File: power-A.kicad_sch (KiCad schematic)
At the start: 28 parts, among them J201 PCB Receptacle, J202 PCB Receptacle, J203 Conn_01x05, U201 AMS1117-ADJ_SOT223

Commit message: Pre routing: footprints&parts
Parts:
- D201: value SMBJ170CA -> TVS Diode; JLCPCB C114013 -> C78395
- D204: value MDD SS14 -> B5819W; footprint Diode_SMD:D_SMA -> Diode_SMD:D_SOD-123; JLCPCB C2480 -> C8598
- D205, D206: value SM4007PL -> B5819W; JLCPCB C64898 -> C8598
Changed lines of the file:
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@@
       (effects (font (size 1.27 1.27)) (justify right))
     )
-    (property "Value" "SMBJ170CA" (id 1) (at 38.735 85.725 0)
+    (property "Value" "TVS Diode" (id 1) (at 38.735 85.725 0)
       (effects (font (size 1.27 1.27)) (justify right))
     )
@@
       (effects (font (size 1.27 1.27)) hide)
     )
-    (property "JLCPCB" "C114013" (id 4) (at 41.91 91.44 0)
+    (property "JLCPCB" "C78395" (id 4) (at 41.91 91.44 0)
       (effects (font (size 1.27 1.27)) hide)
     )
@@
       (effects (font (size 1.27 1.27)) (justify left))
     )
-    (property "Value" "SM4007PL" (id 1) (at 171.45 139.6999 90)
+    (property "Value" "B5819W" (id 1) (at 171.45 139.6999 90)
       (effects (font (size 1.27 1.27)) (justify left))
     )
@@
       (effects (font (size 1.27 1.27)) hide)
     )
-    (property "JLCPCB" "C64898" (id 4) (at 168.275 138.43 0)
+    (property "JLCPCB" "C8598 " (id 4) (at 168.275 138.43 0)
       (effects (font (size 1.27 1.27)) hide)
     )
@@
       (effects (font (size 1.27 1.27)) (justify left))
     )
-    (property "Value" "SM4007PL" (id 1) (at 171.45 129.5399 90)
+    (property "Value" "B5819W" (id 1) (at 171.45 129.5399 90)
       (effects (font (size 1.27 1.27)) (justify left))
     )
@@
       (effects (font (size 1.27 1.27)) hide)
     )
-    (property "JLCPCB" "C64898" (id 4) (at 168.275 128.27 0)
+    (property "JLCPCB" "C8598 " (id 4) (at 168.275 128.27 0)
       (effects (font (size 1.27 1.27)) hide)
     )
@@
     (in_bom yes) (on_board yes)
     (property "Reference" "D204" (id 0) (at 112.395 76.835 0))
-    (property "Value" "MDD SS14" (id 1) (at 111.76 83.82 0))
-    (property "Footprint" "Diode_SMD:D_SMA" (id 2) (at 112.395 80.645 0)
-      (effects (font (size 1.27 1.27)) hide)
-    )
-    (property "Datasheet" "https://datasheet.lcsc.com/lcsc/2204121115_MDD-Microdiode-Electronics--SS14_C2480.pdf" (id 3) (at 112.395 80.645 0)
-      (effects (font (size 1.27 1.27)) hide)
-    )
-    (property "JLCPCB" "C2480" (id 4) (at 112.395 80.645 0)
-      (effects (font (size 1.27 1.27)) hide)
-    )
+    (property "Value" "B5819W" (id 1) (at 111.76 83.82 0))
+    (property "Footprint" "Diode_SMD:D_SOD-123" (id 2) (at 112.395 80.645 0)
+      (effects (font (size 1.27 1.27)) hide)
+    )
+    (property "Datasheet" "" (id 3) (at 112.395 80.645 0)
+      (effects (font (size 1.27 1.27)) hide)
+    )
+    (property "JLCPCB" "C8598 " (id 4) (at 112.395 80.645 0)
+      (effects (font (size 1.27 1.27)) hide)
+    )

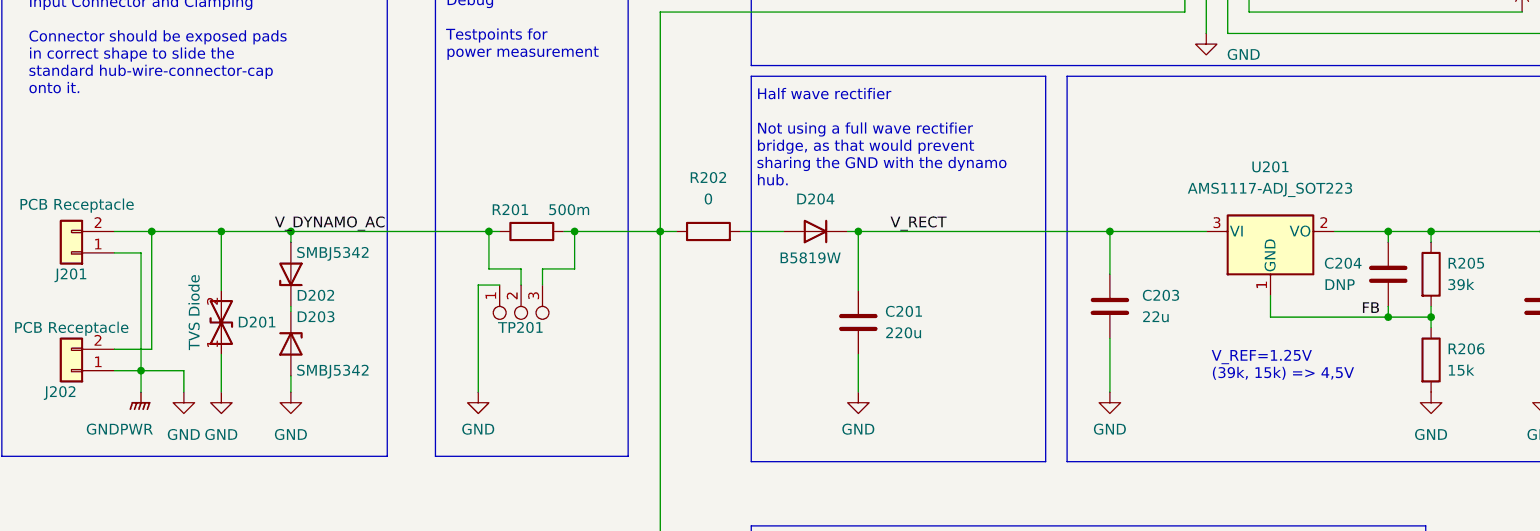
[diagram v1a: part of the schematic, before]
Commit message: Schematics: Add mountingpins to connectors, remove ERC warnings for alternate parts
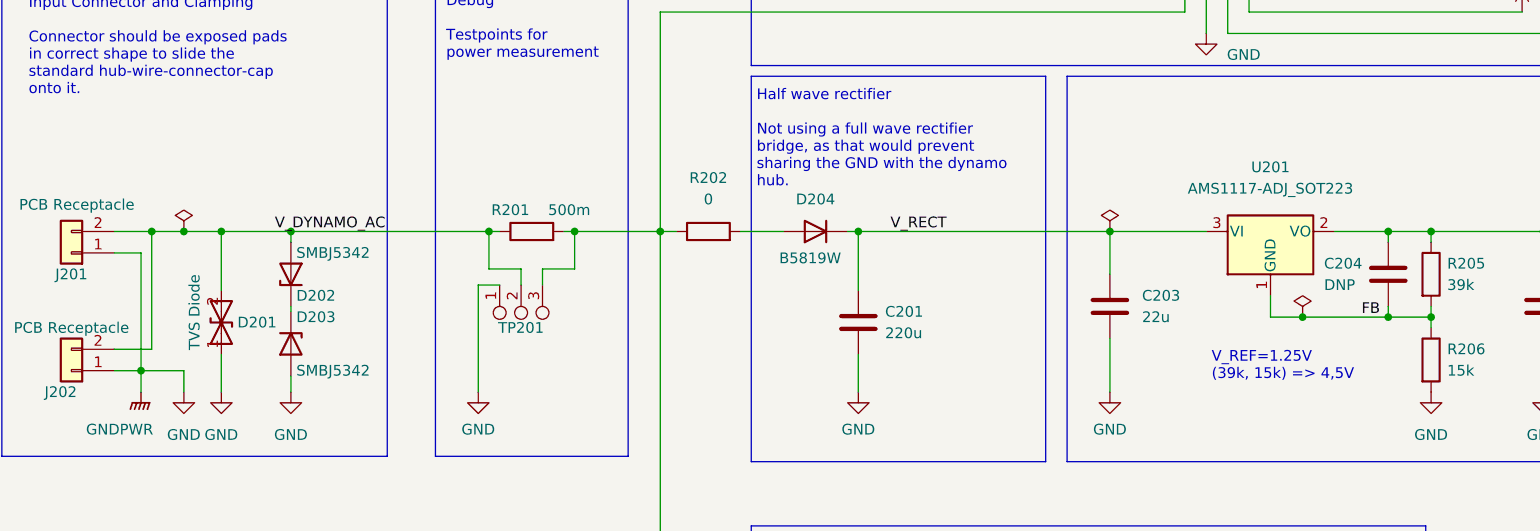
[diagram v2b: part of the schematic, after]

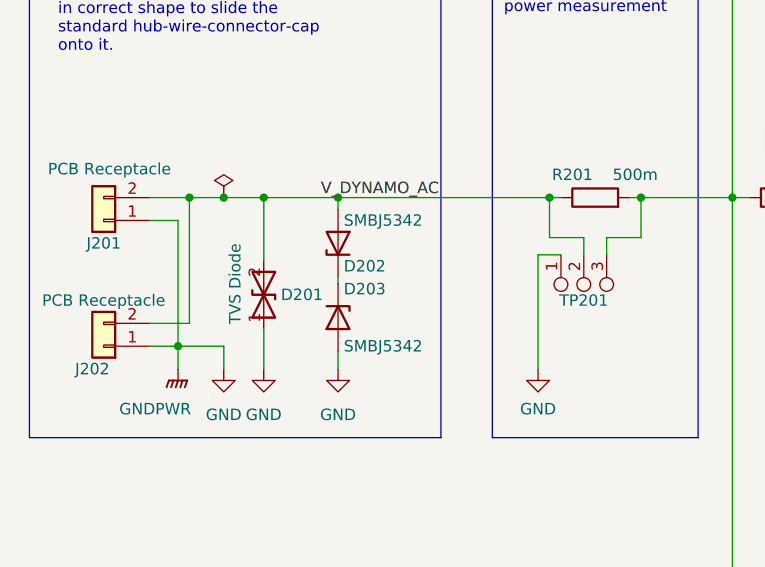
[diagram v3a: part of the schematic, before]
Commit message: schematic: cleanups and diode selection
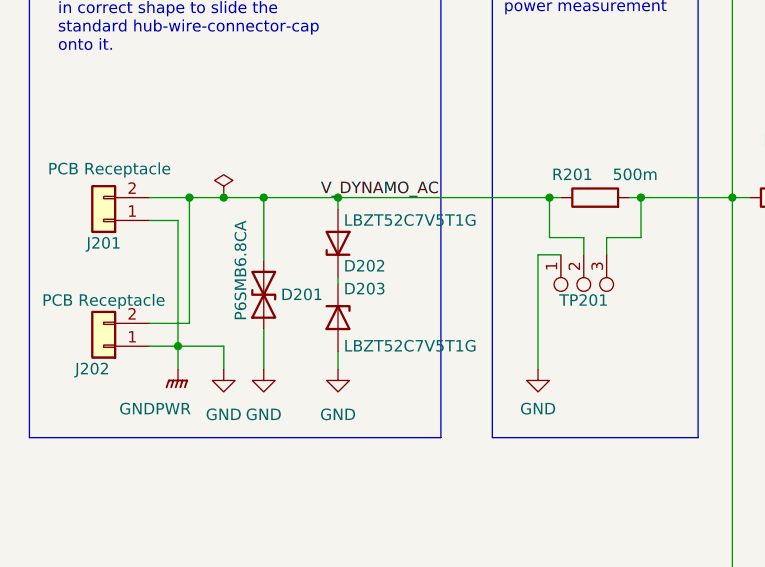
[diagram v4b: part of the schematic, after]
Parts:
- D201: value TVS Diode -> P6SMB6.8CA
- D202, D203: value SMBJ5342 -> LBZT52C7V5T1G; footprint Diode_SMD:D_SMB -> Diode_SMD:D_SOD-123; JLCPCB C132286 -> C12760
- U201: JLCPCB (none) -> C347224
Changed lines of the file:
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@@
       (effects (font (size 1.27 1.27)) (justify left))
     )
-    (property "Value" "SMBJ5342" (id 1) (at 50.8 97.155 90)
-      (effects (font (size 1.27 1.27)) (justify left))
-    )
-    (property "Footprint" "Diode_SMD:D_SMB" (id 2) (at 50.165 93.98 0)
+    (property "Value" "LBZT52C7V5T1G" (id 1) (at 50.8 97.155 90)
+      (effects (font (size 1.27 1.27)) (justify left))
+    )
+    (property "Footprint" "Diode_SMD:D_SOD-123" (id 2) (at 50.165 93.98 0)
       (effects (font (size 1.27 1.27)) hide)
     )
@@
       (effects (font (size 1.27 1.27)) hide)
     )
-    (property "JLCPCB" "C132286" (id 4) (at 50.165 93.98 0)
+    (property "JLCPCB" "C12760" (id 4) (at 50.165 93.98 0)
       (effects (font (size 1.27 1.27)) hide)
     )
@@
       (effects (font (size 1.27 1.27)) (justify right))
     )
-    (property "Value" "TVS Diode" (id 1) (at 38.735 85.725 0)
+    (property "Value" "P6SMB6.8CA" (id 1) (at 39.37 83.185 0)
       (effects (font (size 1.27 1.27)) (justify right))
     )
@@
       (effects (font (size 1.27 1.27)) hide)
     )
-    (property "Datasheet" "" (id 3) (at 168.91 86.995 0)
+    (property "Datasheet" "~" (id 3) (at 168.91 86.995 0)
+      (effects (font (size 1.27 1.27)) hide)
+    )
+    (property "JLCPCB" "C347224" (id 4) (at 166.37 80.645 0)
       (effects (font (size 1.27 1.27)) hide)
     )
@@
       (effects (font (size 1.27 1.27)) hide)
     )
-    (property "Datasheet" "" (id 3) (at 168.275 138.43 0)
+    (property "Datasheet" "~" (id 3) (at 168.275 138.43 0)
       (effects (font (size 1.27 1.27)) hide)
     )
@@
       (effects (font (size 1.27 1.27)) (justify right))
     )
-    (property "Value" "SMBJ5342" (id 1) (at 50.8 83.185 90)
-      (effects (font (size 1.27 1.27)) (justify right))
-    )
-    (property "Footprint" "Diode_SMD:D_SMB" (id 2) (at 50.165 85.725 0)
+    (property "Value" "LBZT52C7V5T1G" (id 1) (at 50.8 83.185 90)
+      (effects (font (size 1.27 1.27)) (justify right))
+    )
+    (property "Footprint" "Diode_SMD:D_SOD-123" (id 2) (at 50.165 85.725 0)
       (effects (font (size 1.27 1.27)) hide)
     )
@@
       (effects (font (size 1.27 1.27)) hide)
     )
-    (property "JLCPCB" "C132286" (id 4) (at 50.165 85.725 0)
+    (property "JLCPCB" "C12760" (id 4) (at 50.165 85.725 0)
       (effects (font (size 1.27 1.27)) hide)
     )
@@
       (effects (font (size 1.27 1.27)) hide)
     )
-    (property "Datasheet" "" (id 3) (at 168.275 128.27 0)
+    (property "Datasheet" "~" (id 3) (at 168.275 128.27 0)
       (effects (font (size 1.27 1.27)) hide)
     )
@@
       (effects (font (size 1.27 1.27)) hide)
     )
-    (property "Datasheet" "" (id 3) (at 112.395 80.645 0)
-      (effects (font (size 1.27 1.27)) hide)
-    )
+    (property "Datasheet" "~" (id 3) (at 112.395 80.645 0)
+      (effects (font (size 1.27 1.27)) hide)
+    )

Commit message: footprints: define testpoint with smaller courtyard
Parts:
- TP201, TP202: footprint Connector_PinHeader_1.27mm:PinHeader_1x03_P1.27mm_Vertical -> project-lib:TestPoint_1x03_P1.27mm
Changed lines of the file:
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@@
       (effects (font (size 1.27 1.27)) hide)
     )
-    (property "Footprint" "Connector_PinHeader_1.27mm:PinHeader_1x03_P1.27mm_Vertical" (id 2) (at 217.297 86.995 0)
+    (property "Footprint" "project-lib:TestPoint_1x03_P1.27mm" (id 2) (at 217.297 86.995 0)
       (effects (font (size 1.27 1.27)) hide)
     )
@@
       (effects (font (size 1.27 1.27)) hide)
     )
-    (property "Footprint" "Connector_PinHeader_1.27mm:PinHeader_1x03_P1.27mm_Vertical" (id 2) (at 75.692 86.995 0)
+    (property "Footprint" "project-lib:TestPoint_1x03_P1.27mm" (id 2) (at 75.692 86.995 0)
       (effects (font (size 1.27 1.27)) hide)
     )

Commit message: schematic: assign connector footprint
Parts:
- J201, J202: footprint (none) -> project-lib:shimano-hub-generator-connector
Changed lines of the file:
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@@
     (property "Reference" "J201" (id 0) (at 24.13 85.725 0))
     (property "Value" "PCB Receptacle" (id 1) (at 24.765 77.47 0))
-    (property "Footprint" "" (id 2) (at 24.13 83.185 0)
+    (property "Footprint" "project-lib:shimano-hub-generator-connector" (id 2) (at 24.13 83.185 0)
       (effects (font (size 1.27 1.27)) hide)
     )
@@
     (property "Reference" "J202" (id 0) (at 22.86 99.695 0))
     (property "Value" "PCB Receptacle" (id 1) (at 24.13 92.075 0))
-    (property "Footprint" "" (id 2) (at 24.13 97.155 0)
-      (effects (font (size 1.27 1.27)) hide)
-    )
+    (property "Footprint" "project-lib:shimano-hub-generator-connector" (id 2) (at 24.13 97.155 0)
+      (effects (font (size 1.27 1.27)) hide)
+    )

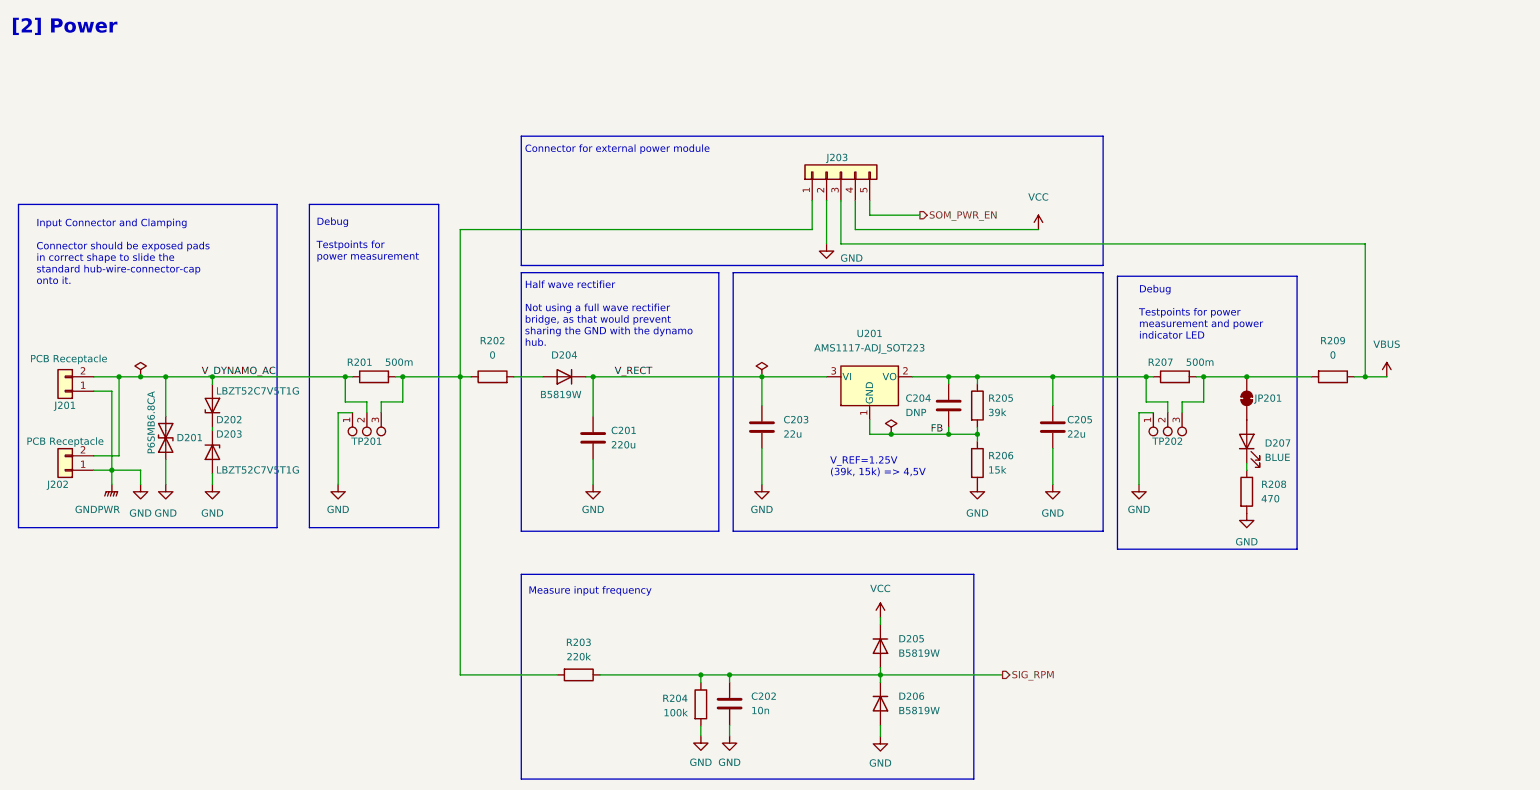
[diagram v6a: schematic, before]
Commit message: Schematic: more 0R resistors and power module connector
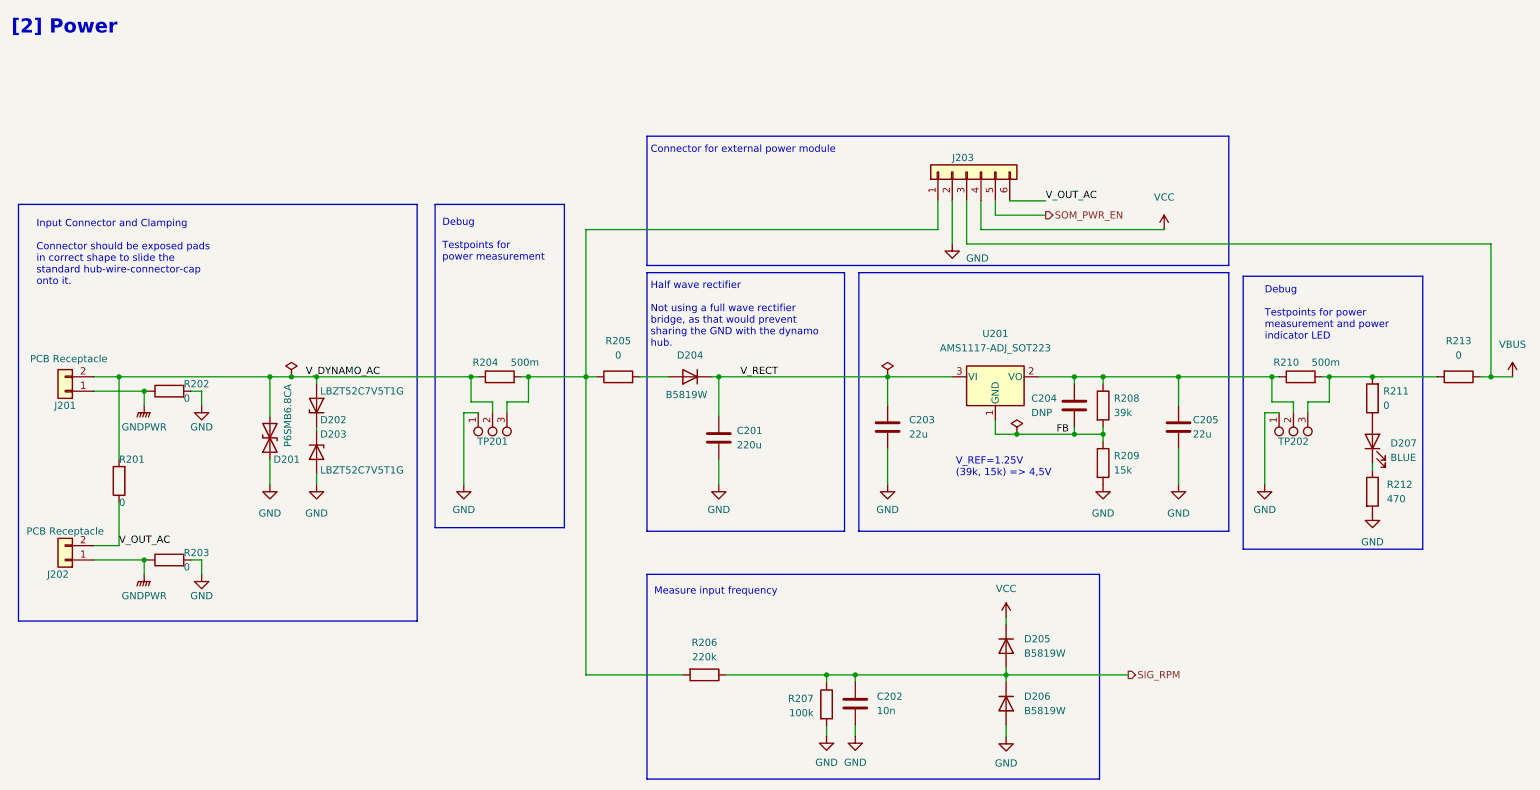
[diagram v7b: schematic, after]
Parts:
- removed JP201: Jumper_2_Bridged, Jumper:SolderJumper-2_P1.3mm_Open_RoundedPad1.0x1.5mm, symbol Jumper:SolderJumper_2_Bridged
- added R201, R202, R203, R211: 0, Resistor_SMD:R_0805_2012Metric_Pad1.20x1.40mm_HandSolder, symbol Device:R
- J203: value Conn_01x05 -> Conn_01x06; footprint (none) -> project-lib:powermodule; symbol Connector_Generic:Conn_01x05 -> Connector_Generic:Conn_01x06
- renumbered R201 to R204, R202 to R205, R203 to R206, R204 to R207, R205 to R208, R206 to R209, R207 to R210, R208 to R212, R209 to R213
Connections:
- net GND: now also R202.2, R203.2; no longer J201.1 (Pin_1), J202.1 (Pin_1)
- net V_DYNAMO_AC: now also R201.2; no longer J202.2 (Pin_2)
- net at R210.2, R213.2, TP202.3: now also R211.2
- net at D207.2 (A): now also R211.1
- new net GNDPWR: J201.1 (Pin_1), J202.1 (Pin_1), R202.1, R203.1
- new net V_OUT_AC: J202.2 (Pin_2), J203.6 (Pin_6), R201.1
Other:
- moved on the sheet: C201, C202, C203, C204, C205, D201, D202, D203, D204, D205, D206, D207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

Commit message: PCB: add powermodule and reroute some stuff
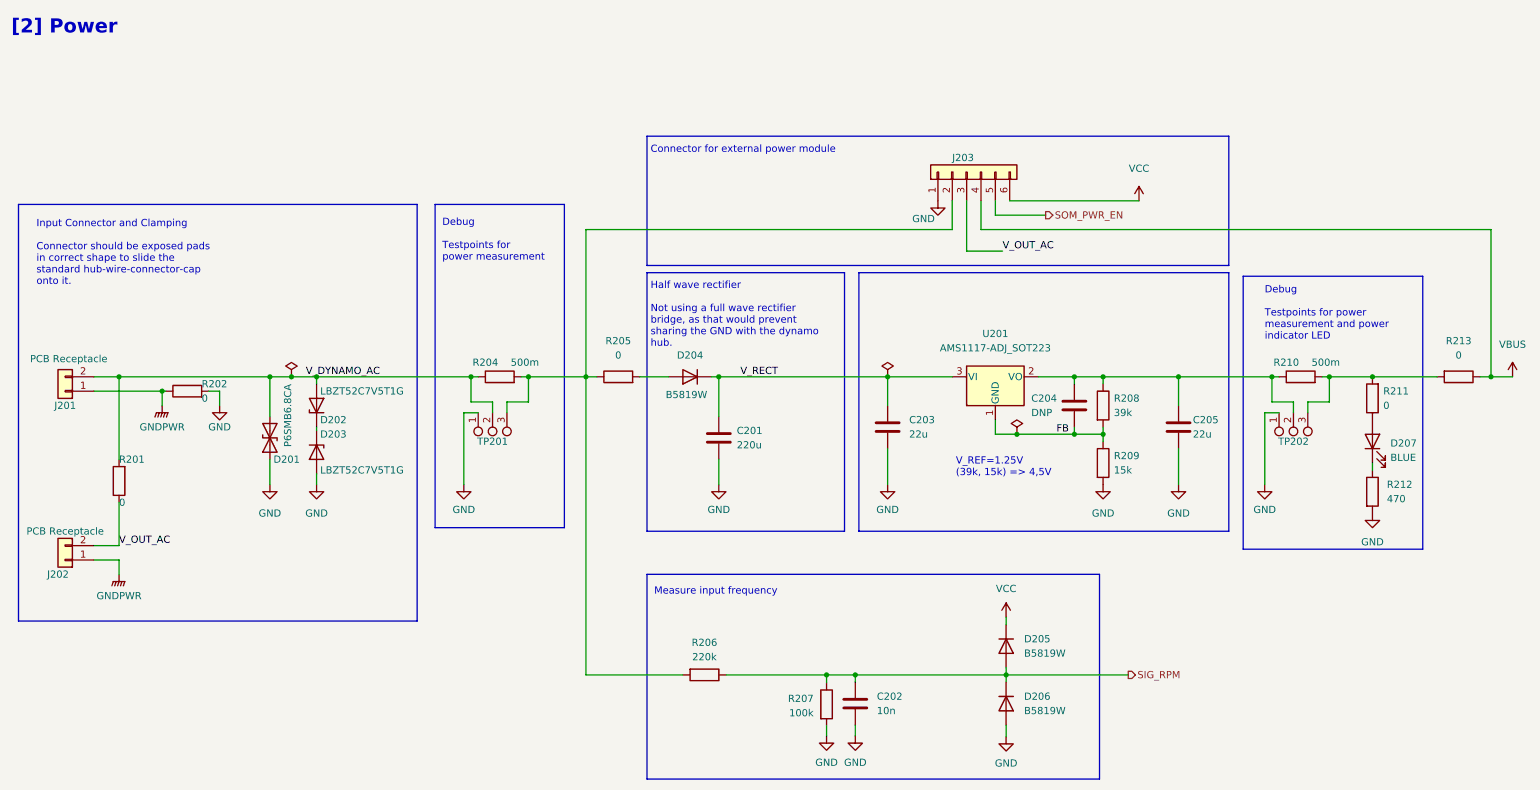
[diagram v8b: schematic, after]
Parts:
- removed R203: 0, Resistor_SMD:R_0805_2012Metric_Pad1.20x1.40mm_HandSolder, symbol Device:R
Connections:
- net GND: now also J203.1 (Pin_1); no longer J203.2 (Pin_2)
- net VBUS: now also J203.4 (Pin_4); no longer J203.3 (Pin_3)
- net VCC: now also J203.6 (Pin_6); no longer J203.4 (Pin_4)
- net V_OUT_AC: now also J203.3 (Pin_3); no longer J203.6 (Pin_6)
- net at R204.2, R205.1, R206.2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: now also J203.2 (Pin_2); no longer J203.1 (Pin_1)
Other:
- moved on the sheet: R202
